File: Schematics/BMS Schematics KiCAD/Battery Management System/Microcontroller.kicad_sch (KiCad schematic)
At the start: 24 parts, among them J3 Boot, SW2 SW_Push, U10 RT9193-33GB, U2 MIC4680, U9 STM32F103C8T6, Y4 CM8V-T1A-32.768KHZ-12.5PF-20P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, Y5 8MHz

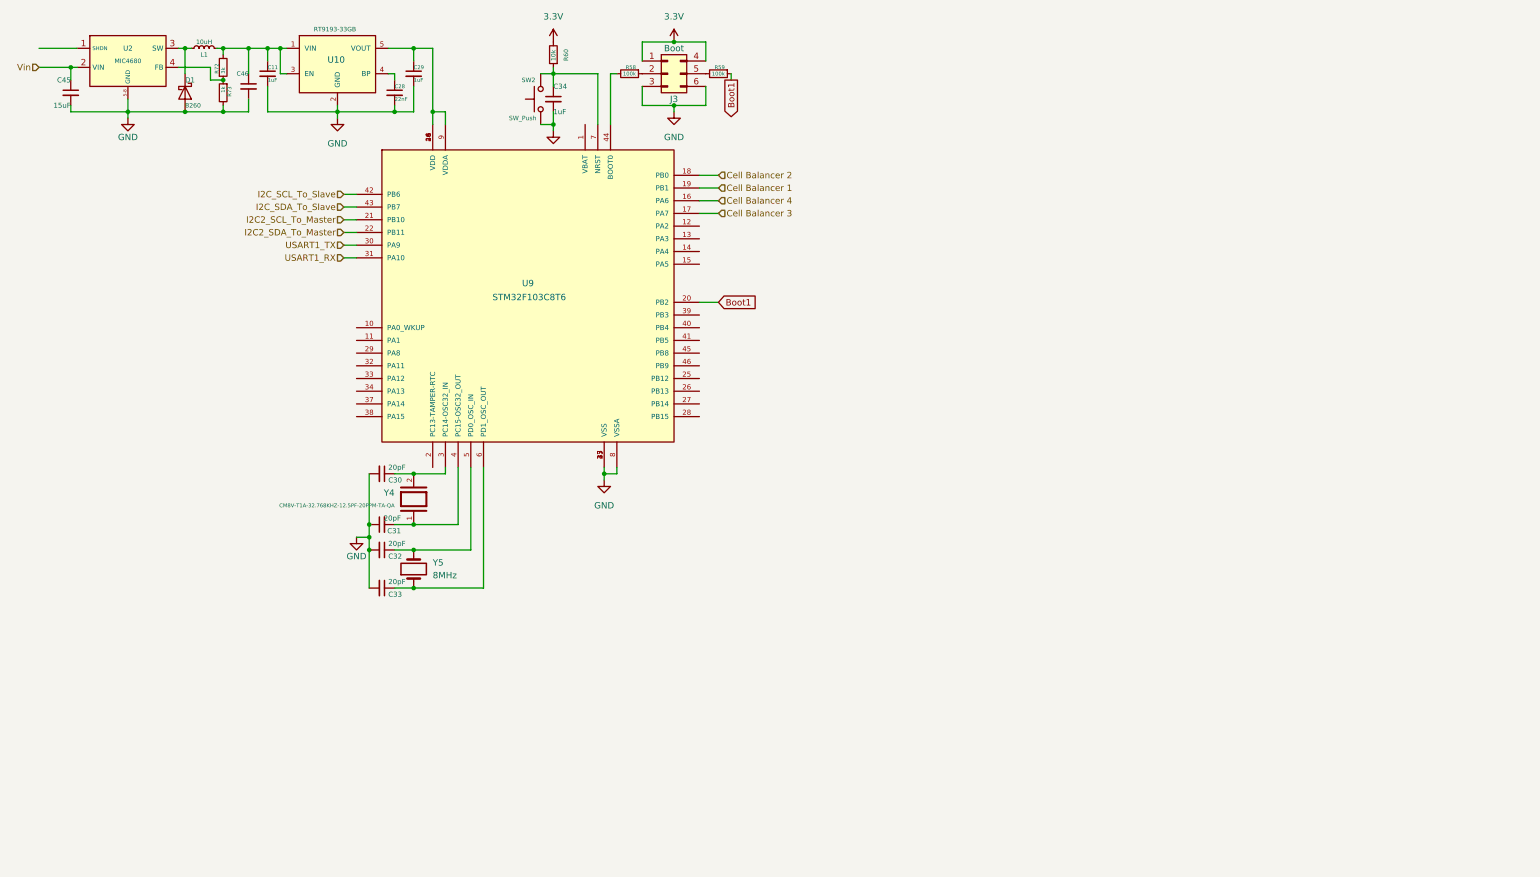
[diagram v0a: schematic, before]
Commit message: Pulled together root sheet so that it's obvious how the power flows and how the blocks are connected. Finally, a decent block diagram :)
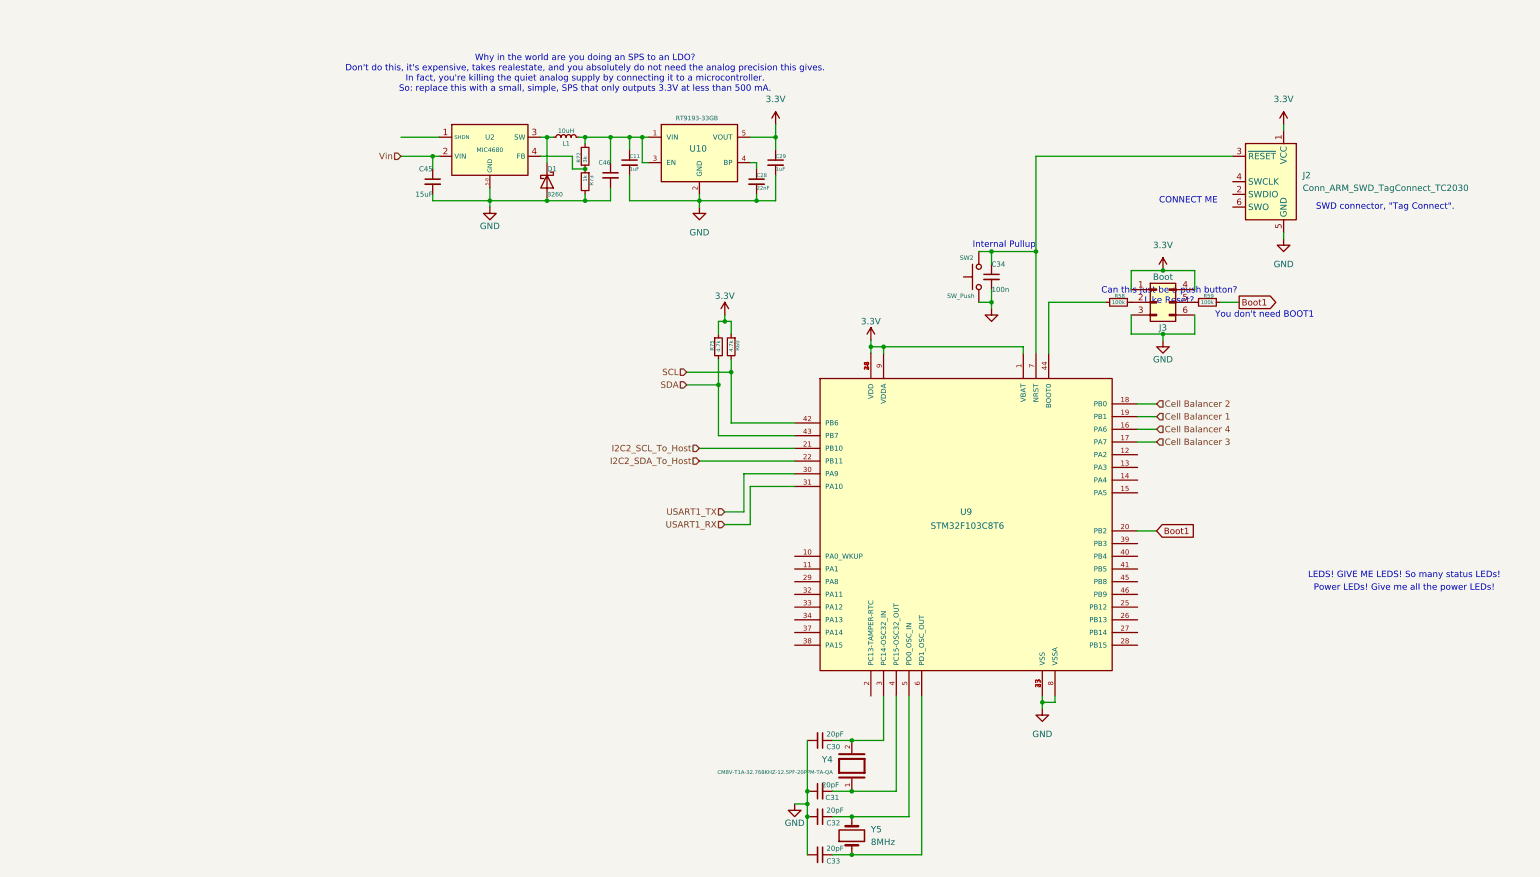
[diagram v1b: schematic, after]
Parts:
- added J2: Conn_ARM_SWD_TagConnect_TC2030, Connector:Tag-Connect_TC2030-IDC-FP_2x03_P1.27mm_Vertical, symbol Connector:Conn_ARM_SWD_TagConnect_TC2030
- added R75: 4.7k, Resistor_SMD:R_0201_0603Metric, symbol Device:R_Small
- C34: value 1uF -> 100n
- R60: value 10k -> 4.7k
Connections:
- net 3.3V: now also C29.1, R60.1, U10.5 (VOUT), U9.1 (VBAT), U9.24 (VDD), U9.36 (VDD), U9.48 (VDD), U9.9 (VDDA), J2.1 (VCC), R75.1; no longer R60.2
- net GND: now also J2.5 (GND)
- net at C34.1, SW2.2, U9.7 (NRST): now also J2.3 (~{RESET}); no longer R60.1
- net I2C2_SCL_To_Master renamed I2C2_SCL_To_Host
- net I2C2_SDA_To_Master renamed I2C2_SDA_To_Host
- net I2C_SCL_To_Slave  renamed SCL
- net SCL: now also R60.2
- net I2C_SDA_To_Slave renamed SDA
- net SDA: now also R75.2
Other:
- note added: "CONNECT ME"
- note added: "Can this just be a push button? Like Reset?"
- note added: "Internal Pullup"
- note added: "LEDS! GIVE ME LEDS! So many status LEDs!"
- note added: "Power LEDs! Give me all the power LEDs!"
- note added: "SWD connector, "Tag Connect"."
- note added: "Why in the world are you doing an SPS to an LDO? Don't do this, it's expensive, takes realestate, and you absolutely do not need the analog precision this gives. In fact, you're killing the quiet analog supply by connecting it to a microcontroller. So: replace this with a small, simple, SPS that only outputs 3.3V at less than 500 mA."
- note added: "You don't need BOOT1"
- moved on the sheet: C11, C28, C29, C30, C31, C32, C33, C34, C45, C46, D1, J3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
